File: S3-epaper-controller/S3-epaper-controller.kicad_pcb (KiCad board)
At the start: 4 copper layers, 115.7 x 70.4 mm, 65 parts, among them P1 CONN_02X13, U1 ESP32-S3-DEVKITC-1-N8R2, U3 QFN50P700X700X100-49N, U6 ED060XC5

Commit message: Update Schematics PDF
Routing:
- net GND: track 126.8 -> 124.5 mm, vias 42 -> 41
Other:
- board text added: "."
- board text added: "3.3V"
- board text added: "> Bottom line unconnected"
- board text added: "GND"
- board text added: "IO17"
- board text added: "IO37"
- board text added: "IO38"
- board text added: "IO45"
- board text added: "IO47"
- board text added: "IO8 SCL"
- board text added: "IO9 SDA"
- board text added: "RX"
- board text added: "TX"
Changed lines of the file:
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@@
     (property "Sheetname" "")
     (attr through_hole)
-    (fp_text reference "P1" (at 1.27 -2.33 90) (layer "F.SilkS")
+    (fp_text reference "P1" (at 2.6 33.08 90) (layer "F.SilkS")
       (effects (font (size 1 1) (thickness 0.15)))
     )
@@
   (gr_line (start 182.44 70.37) (end 182.44 119.9) (layer "Edge.Cuts") (width 0.1))
   (gr_line (start 91.94 49.48) (end 103.87 49.48) (layer "Edge.Cuts") (width 0.1))
+  (gr_text "IO37" (at 83.424998 111.361905 90) (layer "F.SilkS")
+    (effects (font (size 1 1) (thickness 0.15)))
+  )
   (gr_text "-15" (at 140.79 105.78) (layer "F.SilkS")
     (effects (font (size 1 1) (thickness 0.15)))
   )
+  (gr_text "RX" (at 103.758326 112.1 90) (layer "F.SilkS")
+    (effects (font (size 1 1) (thickness 0.15)))
+  )
+  (gr_text "IO17" (at 78.341666 111.361905 90) (layer "F.SilkS")
+    (effects (font (size 1 1) (thickness 0.15)))
+  )
+  (gr_text "IO8 SCL" (at 93.591662 110.07619 90) (layer "F.SilkS")
+    (effects (font (size 1 1) (thickness 0.15)))
+  )
+  (gr_text "." (at 98.333334 112.55 90) (layer "F.SilkS")
+    (effects (font (size 1 1) (thickness 0.15)))
+  )
   (gr_text "+22" (at 173.73 104.45) (layer "F.SilkS")
     (effects (font (size 1 1) (thickness 0.15)))
@@
     (effects (font (size 1 1) (thickness 0.15)))
   )
+  (gr_text "IO45" (at 88.50833 111.361905 90) (layer "F.SilkS")
+    (effects (font (size 1 1) (thickness 0.15)))
+  )
+  (gr_text "." (at 95.791668 112.55 90) (layer "F.SilkS")
+    (effects (font (size 1 1) (thickness 0.15)))
+  )
+  (gr_text "> Bottom line unconnected" (at 115.825 117.55) (layer "F.SilkS")
+    (effects (font (size 0.7 0.7) (thickness 0.12)))
+  )
+  (gr_text "IO38" (at 85.966664 111.361905 90) (layer "F.SilkS")
+    (effects (font (size 1 1) (thickness 0.15)))
+  )
+  (gr_text "TX" (at 106.3 112.219047 90) (layer "F.SilkS")
+    (effects (font (size 1 1) (thickness 0.15)))
+  )
+  (gr_text "GND" (at 73.3 117.625 90) (layer "F.SilkS")
+    (effects (font (size 1 1) (thickness 0.15)))
+  )
   (gr_text "-20" (at 135.54 104.4) (layer "F.SilkS")
     (effects (font (size 1 1) (thickness 0.15)))
   )
+  (gr_text "IO9 SDA" (at 91.049996 110.052381 90) (layer "F.SilkS")
+    (effects (font (size 1 1) (thickness 0.15)))
+  )
   (gr_text "+15" (at 168.39 105.67) (layer "F.SilkS")
+    (effects (font (size 1 1) (thickness 0.15)))
+  )
+  (gr_text "." (at 100.875 112.55 90) (layer "F.SilkS")
+    (effects (font (size 1 1) (thickness 0.15)))
+  )
+  (gr_text "3.3V" (at 75.8 111.457143 90) (layer "F.SilkS")
+    (effects (font (size 1 1) (thickness 0.15)))
+  )
+  (gr_text "IO47" (at 80.883332 111.361905 90) (layer "F.SilkS")
     (effects (font (size 1 1) (thickness 0.15)))
   )
@@
   (segment (start 142.0818 88.8384) (end 142.6268 89.3834) (width 0.5) (layer "F.Cu") (net 1))
   (segment (start 146.92 100.85) (end 146.92 100.78) (width 0.4) (layer "F.Cu") (net 1))
-  (segment (start 75.82 117.5) (end 74.48 117.5) (width 0.25) (layer "F.Cu") (net 1))
   (segment (start 144.16 106.13) (end 142.75 106.13) (width 0.4) (layer "F.Cu") (net 1))
   (segment (start 169.33 95.325) (end 169.32 95.315) (width 0.4) (layer "F.Cu") (net 1))
@@
   (segment (start 142.0818 88.6514) (end 140.9758 88.6514) (width 0.5) (layer "F.Cu") (net 1))
   (segment (start 157.744081 90.516681) (end 157.744081 91.468063) (width 0.25) (layer "F.Cu") (net 1))
-  (segment (start 74.48 117.5) (end 73.81 118.17) (width 0.25) (layer "F.Cu") (net 1))
   (segment (start 157.2308 76.7794) (end 160.9808 76.7794) (width 1) (layer "F.Cu") (net 1))
   (segment (start 163.3648 79.062893) (end 163.3648 77.2374) (width 0.25) (layer "F.Cu") (net 1))
@@
   (via (at 148.8148 86.6954) (size 0.8) (drill 0.4) (layers "F.Cu" "B.Cu") (net 1))
   (via (at 162.6648 89.4374) (size 0.8) (drill 0.4) (layers "F.Cu" "B.Cu") (net 1))
-  (via (at 73.81 118.17) (size 0.65) (drill 0.4) (layers "F.Cu" "B.Cu") (net 1))
   (via (at 153.04 112.65) (size 0.65) (drill 0.4) (layers "F.Cu" "B.Cu") (net 1))
   (via (at 141.63 78.52) (size 0.7) (drill 0.4) (layers "F.Cu" "B.Cu") (net 1))

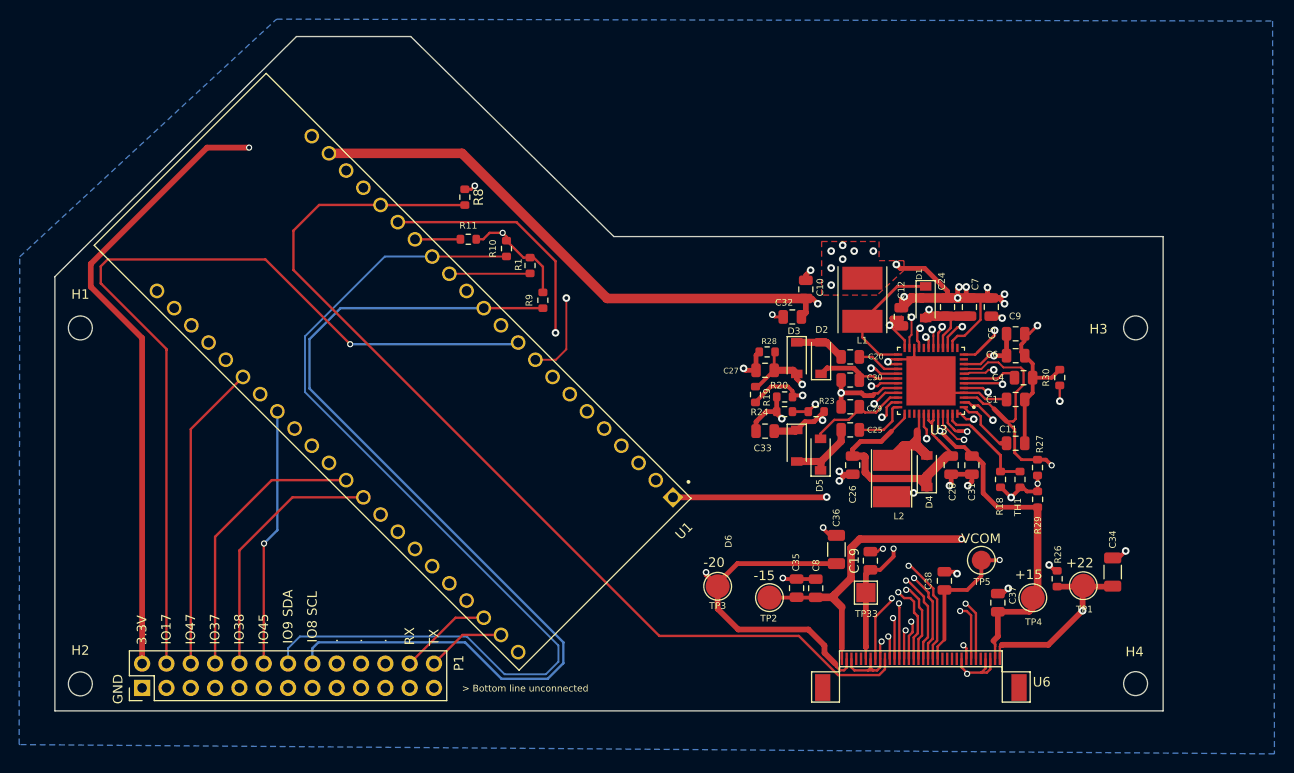
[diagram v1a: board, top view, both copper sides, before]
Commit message: REF https://github.com/martinberlin/epdiy-rotation/issues/6 Do not use IO46 (strapping pin)
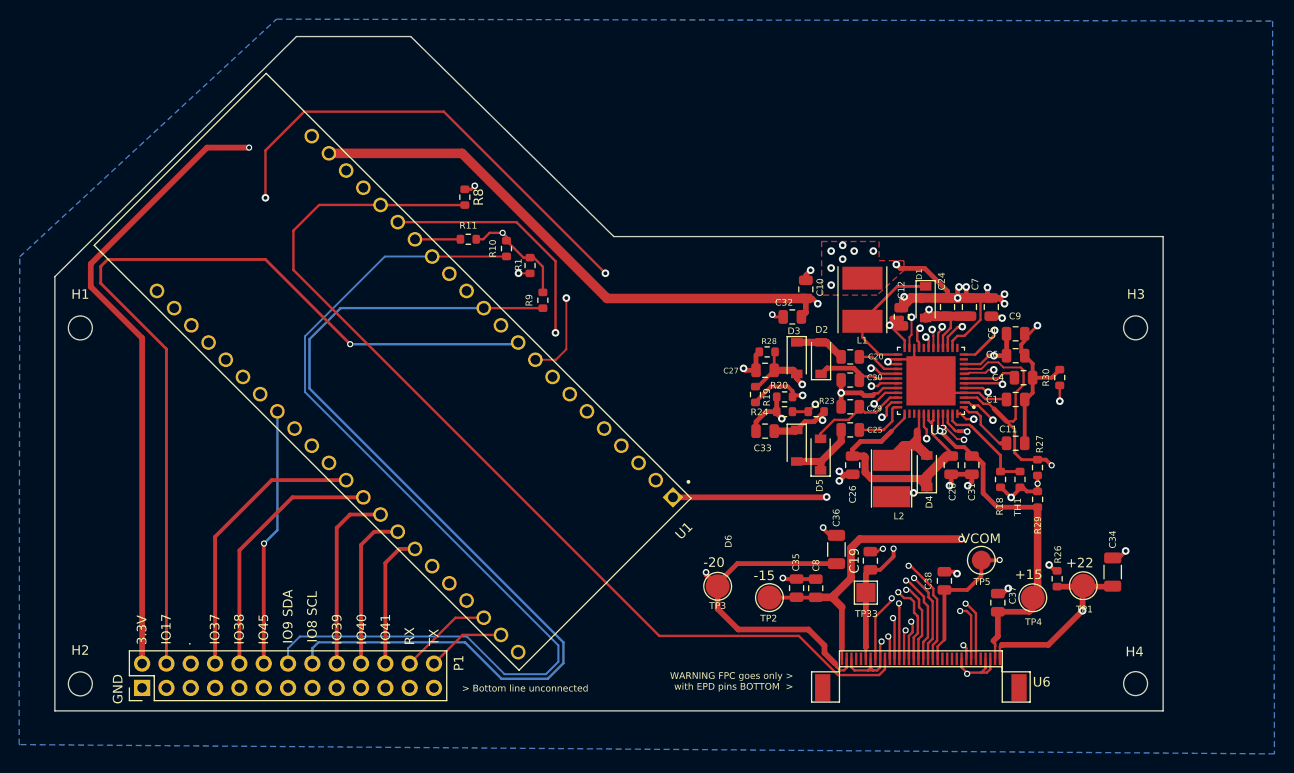
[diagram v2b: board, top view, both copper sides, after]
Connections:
- P1 pad 18: unconnected-(P1-Pad18) -> /IO39
- P1 pad 20: unconnected-(P1-Pad20) -> /IO40
- P1 pad 22: unconnected-(P1-Pad22) -> /IO41
- P1 pad 6: /IO47 -> unconnected-(P1-Pad6)
- U1 pad J1_14: /TPS_PWR_GOOD -> unconnected-(U1-PadJ1_14)
- U1 pad J3_17: /IO47 -> /TPS_PWR_GOOD
- U1 pad J3_7: unconnected-(U1-PadJ3_7) -> /IO41
- U1 pad J3_8: unconnected-(U1-PadJ3_8) -> /IO40
- U1 pad J3_9: unconnected-(U1-PadJ3_9) -> /IO39
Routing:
- net /TPS_PWR_GOOD: track 64.8 -> 137.1 mm, vias 1 -> 4
- net /IO47: track 32.2 -> 0.00 mm
- net /IO39: track 0.00 -> 19.3 mm
- net /IO40: track 0.00 -> 16.8 mm
- net /IO41: track 0.00 -> 14.2 mm
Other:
- board text added: "IO39"
- board text added: "IO40"
- board text added: "IO41"
- board text added: "WARNING FPC goes only > with EPD pins BOTTOM >"
- board text removed: "IO47"

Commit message: Update some IOs + documentation
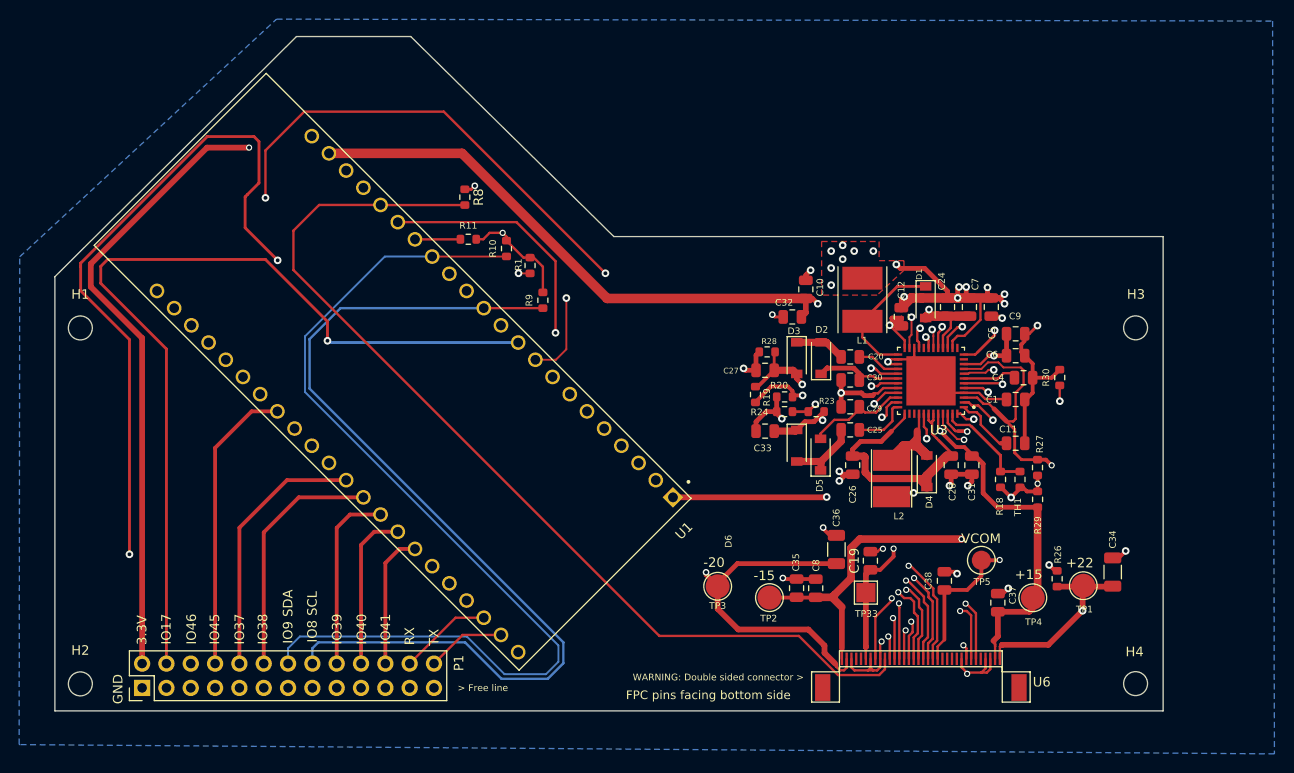
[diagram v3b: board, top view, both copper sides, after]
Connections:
- P1 pad 10: /IO38 -> /IO37
- P1 pad 12: /IO45 -> /IO38
- P1 pad 6: unconnected-(P1-Pad6) -> /IO46
- P1 pad 8: /IO37 -> /IO45
- U1 pad J1_14: unconnected-(U1-PadJ1_14) -> /IO46
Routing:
- net /IO46: track 0.00 -> 103.8 mm, vias 0 -> 2
- net /IO45: track 26.9 -> 30.6 mm, vias 1 -> 0
- net /IO37: track 29.4 -> 27.4 mm
- net /IO38: track 27.1 -> 25.6 mm
- net /IO17: track 91.9 -> 93.0 mm
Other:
- board text added: "> Free line"
- board text added: "FPC pins facing bottom side"
- board text added: "IO46"
- board text added: "WARNING: Double sided connector >"
- board text removed: "."
- board text removed: "> Bottom line unconnected"
- board text removed: "WARNING FPC goes only > with EPD pins BOTTOM >"
